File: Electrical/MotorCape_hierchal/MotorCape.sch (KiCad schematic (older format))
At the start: 9 parts, among them J11 flag_wheel servo, J7 i2c bus connector, P13 battery_connector, P14 Pi_Connector, U1 IMU

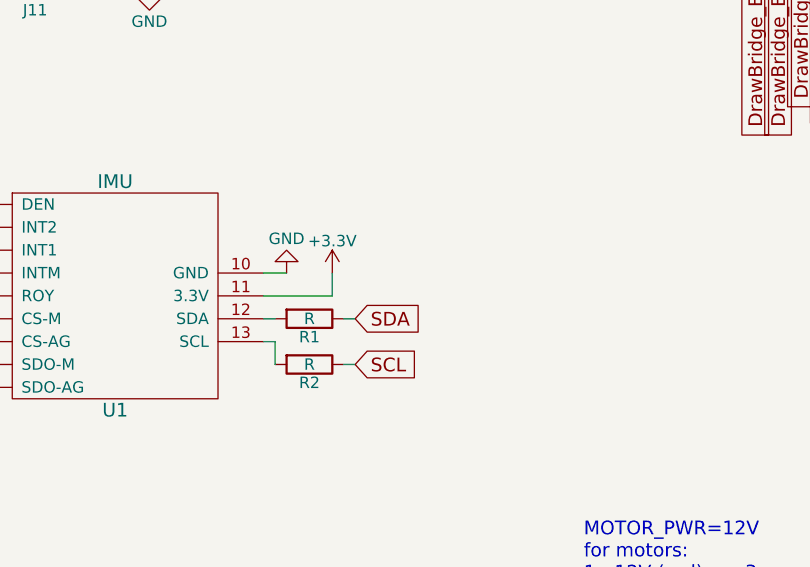
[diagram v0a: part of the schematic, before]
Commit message: trying to lay-out things. lots of via's, this could be a bit messy
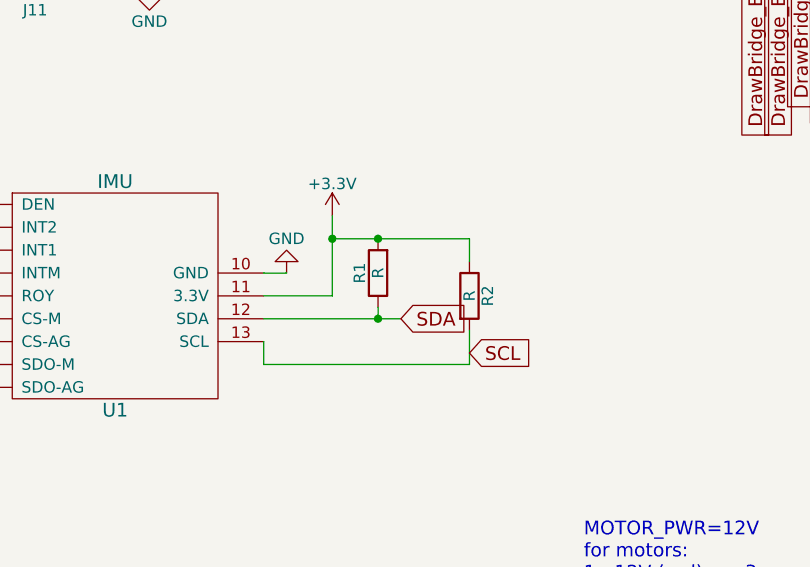
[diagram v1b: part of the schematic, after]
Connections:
- net +3V3: now also R1.2, R2.1
- net SCL: now also R2.2, U1.13 (SCL); no longer R2.1
- net SDA: now also U1.12 (SDA)
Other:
- moved on the sheet: R1, R2
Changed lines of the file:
@@
 NoConn ~ 4300 5900
 NoConn ~ 4300 6000
-Text GLabel 6000 5700 2    60   Input ~ 0
+Text GLabel 6200 5700 2    60   Input ~ 0
 SDA
-Text GLabel 6000 5900 2    60   Input ~ 0
+Text GLabel 6500 5850 2    60   Input ~ 0
 SCL
 $Comp
@@
 L R R2
 U 1 1 5ACFD3ED
-P 5800 5900
-F 0 "R2" V 5880 5900 50  0000 C CNN
-F 1 "R" V 5800 5900 50  0000 C CNN
-F 2 "Resistors_THT:R_Axial_DIN0204_L3.6mm_D1.6mm_P5.08mm_Horizontal" V 5730 5900 50  0001 C CNN
-F 3 "" H 5800 5900 50  0001 C CNN
-	1    5800 5900
-	0    1    1    0
-$EndComp
-$Comp
-L R R1
-U 1 1 5ACFD510
-P 5800 5700
-F 0 "R1" V 5880 5700 50  0000 C CNN
-F 1 "R" V 5800 5700 50  0000 C CNN
-F 2 "Resistors_THT:R_Axial_DIN0204_L3.6mm_D1.6mm_P5.08mm_Horizontal" V 5730 5700 50  0001 C CNN
-F 3 "" H 5800 5700 50  0001 C CNN
-	1    5800 5700
-	0    1    1    0
+P 6500 5600
+F 0 "R2" V 6580 5600 50  0000 C CNN
+F 1 "R" V 6500 5600 50  0000 C CNN
+F 2 "Resistors_THT:R_Axial_DIN0204_L3.6mm_D1.6mm_P5.08mm_Horizontal" V 6430 5600 50  0001 C CNN
+F 3 "" H 6500 5600 50  0001 C CNN
+	1    6500 5600
+	1    0    0    -1
 $EndComp
 Text GLabel 10550 1400 1    60   Input ~ 0
@@
 L +3.3V #PWR011
 U 1 1 5ACCD4EB
-P 5900 5500
-F 0 "#PWR011" H 5900 5350 50  0001 C CNN
-F 1 "+3.3V" H 5900 5640 50  0000 C CNN
-F 2 "" H 5900 5500 50  0001 C CNN
-F 3 "" H 5900 5500 50  0001 C CNN
-	1    5900 5500
+P 5900 5250
+F 0 "#PWR011" H 5900 5100 50  0001 C CNN
+F 1 "+3.3V" H 5900 5390 50  0000 C CNN
+F 2 "" H 5900 5250 50  0001 C CNN
+F 3 "" H 5900 5250 50  0001 C CNN
+	1    5900 5250
 	1    0    0    -1
 $EndComp
@@
 	5700 5500 5600 5500
 Wire Wire Line
-	5900 5500 5900 5600
+	5900 5250 5900 5600
 Wire Wire Line
 	5900 5600 5600 5600
 Wire Wire Line
-	5650 5700 5600 5700
-Wire Wire Line
-	5600 5800 5650 5800
-Wire Wire Line
-	5650 5800 5650 5900
-Wire Wire Line
-	6000 5700 5950 5700
-Wire Wire Line
-	6000 5900 5950 5900
+	5600 5700 6200 5700
 Wire Wire Line
 	5050 3900 5000 3900
@@
 	0    1    1    0
 $EndComp
+$Comp
+L R R1
+U 1 1 5ACFD510
+P 6100 5500
+F 0 "R1" V 6180 5500 50  0000 C CNN
+F 1 "R" V 6100 5500 50  0000 C CNN
+F 2 "Resistors_THT:R_Axial_DIN0204_L3.6mm_D1.6mm_P5.08mm_Horizontal" V 6030 5500 50  0001 C CNN
+F 3 "" H 6100 5500 50  0001 C CNN
+	1    6100 5500
+	-1   0    0    1
+$EndComp
+Wire Wire Line
+	5900 5350 6500 5350
+Connection ~ 5900 5350
+Wire Wire Line
+	6100 5650 6100 5700
+Connection ~ 6100 5700
+Wire Wire Line
+	6500 5900 6500 5750
+Wire Wire Line
+	6500 5350 6500 5450
+Connection ~ 6100 5350
+Wire Wire Line
+	5600 5900 6500 5900
+Wire Wire Line
+	5600 5800 5600 5900
 $EndSCHEMATC

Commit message: pushing changes while routing. still not done yet
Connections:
- net BackLeft_DIR: now also ARD1.59 (D28); no longer ARD1.56 (D25)
- net BackLeft_ENC_A: now also ARD1.61 (D30); no longer ARD1.57 (D26)
- net BackLeft_ENC_B: now also ARD1.63 (D32); no longer ARD1.58 (D27)
- net BackRight_DIR: now also ARD1.71 (D40); no longer ARD1.62 (D31)
- net BackRight_ENC_A: now also ARD1.73 (D42); no longer ARD1.63 (D32)
- net BackRight_ENC_B: now also ARD1.75 (D44); no longer ARD1.64 (D33)
- net DrawBridge_DIR: now also ARD1.82 (D51); no longer ARD1.68 (D37)
- net DrawBridge_ENC_A: now also ARD1.83 (D52_CS2); no longer ARD1.69 (D38)
- net DrawBridge_ENC_B: now also ARD1.84 (D53); no longer ARD1.70 (D39)
- net FlagWheel_DIR: now also ARD1.77 (D46); no longer ARD1.65 (D34)
- net FlagWheel_ENC_A: now also ARD1.79 (D48); no longer ARD1.66 (D35)
- net FlagWheel_ENC_B: now also ARD1.81 (D50); no longer ARD1.67 (D36)
- net FrontLeft_ENC_A: now also ARD1.55 (D24); no longer ARD1.54 (D23)
- net FrontLeft_ENC_B: now also ARD1.57 (D26); no longer ARD1.55 (D24)
- net FrontRight_DIR: now also ARD1.65 (D34); no longer ARD1.59 (D28)
- net FrontRight_ENC_A: now also ARD1.67 (D36); no longer ARD1.60 (D29)
- net FrontRight_ENC_B: now also ARD1.69 (D38); no longer ARD1.61 (D30)
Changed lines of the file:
@@
 	-1   0    0    -1
 $EndComp
-NoConn ~ 6350 4000
-NoConn ~ 6450 4000
-NoConn ~ 6550 4000
-NoConn ~ 6650 4000
 NoConn ~ 6750 4000
-NoConn ~ 6850 4000
 NoConn ~ 6950 4000
-NoConn ~ 7050 4000
 NoConn ~ 7150 4000
-NoConn ~ 7250 4000
 NoConn ~ 7350 4000
-NoConn ~ 7450 4000
 NoConn ~ 7550 4000
-NoConn ~ 7650 4000
 NoConn ~ 9550 4000
 NoConn ~ 9650 4000
-NoConn ~ 9750 4000
-NoConn ~ 9850 4000
-NoConn ~ 9950 4000
 NoConn ~ 6350 1400
 NoConn ~ 6450 1400
@@
 Text GLabel 10650 4000 3    60   Input ~ 0
 FrontLeft_SPD
-Text GLabel 9150 4000 3    60   Input ~ 0
+Text GLabel 8850 4000 3    60   Input ~ 0
 BackLeft_DIR
 Text GLabel 10550 4000 3    60   Input ~ 0
 BackLeft_SPD
-Text GLabel 9350 4000 3    60   Input ~ 0
+Text GLabel 9250 4000 3    60   Input ~ 0
 FrontLeft_ENC_A
-Text GLabel 9250 4000 3    60   Input ~ 0
+Text GLabel 9050 4000 3    60   Input ~ 0
 FrontLeft_ENC_B
-Text GLabel 9050 4000 3    60   Input ~ 0
+Text GLabel 8650 4000 3    60   Input ~ 0
 BackLeft_ENC_A
-Text GLabel 8950 4000 3    60   Input ~ 0
+Text GLabel 8450 4000 3    60   Input ~ 0
 BackLeft_ENC_B
 Text GLabel 10450 4000 3    60   Input ~ 0
@@
 Text GLabel 10350 4000 3    60   Input ~ 0
 BackRight_SPD
-Text GLabel 8250 4000 3    60   Input ~ 0
+Text GLabel 7050 4000 3    60   Input ~ 0
 FlagWheel_DIR
 Text GLabel 10250 4000 3    60   Input ~ 0
 FlagWheel_SPD
-Text GLabel 7950 4000 3    60   Input ~ 0
+Text GLabel 6550 4000 3    60   Input ~ 0
 DrawBridge_DIR
 Text GLabel 10150 4000 3    60   Input ~ 0
 DrawBridge_SPD
-Text GLabel 8150 4000 3    60   Input ~ 0
+Text GLabel 6850 4000 3    60   Input ~ 0
 FlagWheel_ENC_A
+Text GLabel 6650 4000 3    60   Input ~ 0
+FlagWheel_ENC_B
+Text GLabel 6450 4000 3    60   Input ~ 0
+DrawBridge_ENC_A
+Text GLabel 6350 4000 3    60   Input ~ 0
+DrawBridge_ENC_B
+Text GLabel 8250 4000 3    60   Input ~ 0
+FrontRight_DIR
 Text GLabel 8050 4000 3    60   Input ~ 0
-FlagWheel_ENC_B
+FrontRight_ENC_A
 Text GLabel 7850 4000 3    60   Input ~ 0
-DrawBridge_ENC_A
-Text GLabel 7750 4000 3    60   Input ~ 0
-DrawBridge_ENC_B
-Text GLabel 8850 4000 3    60   Input ~ 0
-FrontRight_DIR
-Text GLabel 8750 4000 3    60   Input ~ 0
-FrontRight_ENC_A
-Text GLabel 8650 4000 3    60   Input ~ 0
 FrontRight_ENC_B
-Text GLabel 8550 4000 3    60   Input ~ 0
+Text GLabel 7650 4000 3    60   Input ~ 0
 BackRight_DIR
-Text GLabel 8450 4000 3    60   Input ~ 0
+Text GLabel 7450 4000 3    60   Input ~ 0
 BackRight_ENC_A
-Text GLabel 8350 4000 3    60   Input ~ 0
+Text GLabel 7250 4000 3    60   Input ~ 0
 BackRight_ENC_B
 Text GLabel 10050 4000 3    60   Input ~ 0
@@
 	7250 1150 7250 1400
 $Comp
+L R R1
+U 1 1 5ACFD510
+P 6100 5500
+F 0 "R1" V 6180 5500 50  0000 C CNN
+F 1 "R" V 6100 5500 50  0000 C CNN
+F 2 "Resistors_THT:R_Axial_DIN0204_L3.6mm_D1.6mm_P5.08mm_Horizontal" V 6030 5500 50  0001 C CNN
+F 3 "" H 6100 5500 50  0001 C CNN
+	1    6100 5500
+	-1   0    0    1
+$EndComp
+Wire Wire Line
+	5900 5350 6500 5350
+Connection ~ 5900 5350
+Wire Wire Line
+	6100 5650 6100 5700
+Connection ~ 6100 5700
+Wire Wire Line
+	6500 5900 6500 5750
+Wire Wire Line
+	6500 5350 6500 5450
+Connection ~ 6100 5350
+Wire Wire Line
+	5600 5900 6500 5900
+Wire Wire Line
+	5600 5800 5600 5900
+NoConn ~ 7750 4000
+NoConn ~ 7950 4000
+NoConn ~ 8150 4000
+NoConn ~ 8350 4000
+NoConn ~ 8550 4000
+NoConn ~ 8750 4000
+NoConn ~ 8950 4000
+NoConn ~ 9150 4000
+NoConn ~ 9350 4000
+NoConn ~ 9750 4000
+$Comp
 L Arduino_Due_Shield ARD1
 U 1 1 5AC90C45
@@
 	0    1    1    0
 $EndComp
-$Comp
-L R R1
-U 1 1 5ACFD510
-P 6100 5500
-F 0 "R1" V 6180 5500 50  0000 C CNN
-F 1 "R" V 6100 5500 50  0000 C CNN
-F 2 "Resistors_THT:R_Axial_DIN0204_L3.6mm_D1.6mm_P5.08mm_Horizontal" V 6030 5500 50  0001 C CNN
-F 3 "" H 6100 5500 50  0001 C CNN
-	1    6100 5500
-	-1   0    0    1
-$EndComp
-Wire Wire Line
-	5900 5350 6500 5350
-Connection ~ 5900 5350
-Wire Wire Line
-	6100 5650 6100 5700
-Connection ~ 6100 5700
-Wire Wire Line
-	6500 5900 6500 5750
-Wire Wire Line
-	6500 5350 6500 5450
-Connection ~ 6100 5350
-Wire Wire Line
-	5600 5900 6500 5900
-Wire Wire Line
-	5600 5800 5600 5900
+NoConn ~ 9850 4000
+NoConn ~ 9950 4000
 $EndSCHEMATC

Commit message: pushing latest motor controller layout changes
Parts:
- removed J7: i2c bus connector, MotorCapeComponents:Pin_Header_Latched_1x02, symbol Conn_01x02
- renumbered P14 to Pi_Bus1, J11 to servo1
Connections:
- net BackRight_DIR: now also ARD1.82 (D51); no longer ARD1.71 (D40)
- net BackRight_ENC_A: now also ARD1.83 (D52_CS2); no longer ARD1.73 (D42)
- net BackRight_ENC_B: now also ARD1.84 (D53); no longer ARD1.75 (D44)
- net DrawBridge_DIR: now also ARD1.73 (D42); no longer ARD1.82 (D51)
- net DrawBridge_ENC_A: now also ARD1.75 (D44); no longer ARD1.83 (D52_CS2)
- net DrawBridge_ENC_B: now also ARD1.77 (D46); no longer ARD1.84 (D53)
- net FlagWheel_DIR: now also ARD1.67 (D36); no longer ARD1.77 (D46)
- net FlagWheel_ENC_A: now also ARD1.69 (D38); no longer ARD1.79 (D48)
- net FlagWheel_ENC_B: now also ARD1.71 (D40); no longer ARD1.81 (D50)
- net FrontRight_ENC_A: now also ARD1.79 (D48); no longer ARD1.67 (D36)
- net FrontRight_ENC_B: now also ARD1.81 (D50); no longer ARD1.69 (D38)
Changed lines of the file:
@@
 MOTOR_PWR=12V\nfor motors:\n1 - 12V (red)       3 - encoder gnd(green)       5 - encoder A (yellow)\n2 - Gnd (black)     4 - encoder Vcc(5V)(blue)    6 - encoder B (white)\n
 $Comp
-L Conn_01x02 J7
-U 1 1 59FC44BE
-P 4550 2450
-F 0 "J7" H 4550 2250 50  0000 C CNN
-F 1 "i2c bus connector" H 4600 2600 50  0000 C CNN
-F 2 "MotorCapeComponents:Pin_Header_Latched_1x02" H 4550 2450 50  0001 C CNN
-F 3 "" H 4550 2450 50  0001 C CNN
-	1    4550 2450
-	-1   0    0    -1
-$EndComp
-$Comp
-L Conn_01x03 J11
+L Conn_01x03 servo1
 U 1 1 5A0ED002
 P 4600 4150
-F 0 "J11" H 4600 3950 50  0000 C CNN
+F 0 "servo1" H 4600 3950 50  0000 C CNN
 F 1 "flag_wheel servo" H 4550 4350 50  0000 C CNN
 F 2 "MotorCapeComponents:Pin_Header_Latched_1x03" H 4600 4150 50  0001 C CNN
@@
 NoConn ~ 10050 1400
 NoConn ~ 9950 1400
-Text GLabel 4800 2450 2    60   Input ~ 0
-SCL
-Text GLabel 4800 2550 2    60   Input ~ 0
-SDA
 Text GLabel 9550 1400 1    60   Input ~ 0
 SCL
@@
 NoConn ~ 7650 1500
 $Comp
-L CONN_01X04 P14
+L CONN_01X04 Pi_Bus1
 U 1 1 5AA1DD33
 P 4550 3150
-F 0 "P14" H 4550 2900 50  0000 C CNN
+F 0 "Pi_Bus1" H 4550 2900 50  0000 C CNN
 F 1 "Pi_Connector" H 4550 3400 50  0000 C CNN
 F 2 "MotorCapeComponents:Pin_Header_Latched_1x04" H 4550 3150 50  0001 C CNN
@@
 Text GLabel 10350 4000 3    60   Input ~ 0
 BackRight_SPD
-Text GLabel 7050 4000 3    60   Input ~ 0
+Text GLabel 8050 4000 3    60   Input ~ 0
 FlagWheel_DIR
 Text GLabel 10250 4000 3    60   Input ~ 0
 FlagWheel_SPD
-Text GLabel 6550 4000 3    60   Input ~ 0
+Text GLabel 7450 4000 3    60   Input ~ 0
 DrawBridge_DIR
 Text GLabel 10150 4000 3    60   Input ~ 0
 DrawBridge_SPD
-Text GLabel 6850 4000 3    60   Input ~ 0
+Text GLabel 7850 4000 3    60   Input ~ 0
 FlagWheel_ENC_A
-Text GLabel 6650 4000 3    60   Input ~ 0
+Text GLabel 7650 4000 3    60   Input ~ 0
 FlagWheel_ENC_B
-Text GLabel 6450 4000 3    60   Input ~ 0
+Text GLabel 7250 4000 3    60   Input ~ 0
 DrawBridge_ENC_A
-Text GLabel 6350 4000 3    60   Input ~ 0
+Text GLabel 7050 4000 3    60   Input ~ 0
 DrawBridge_ENC_B
 Text GLabel 8250 4000 3    60   Input ~ 0
 FrontRight_DIR
-Text GLabel 8050 4000 3    60   Input ~ 0
+Text GLabel 6850 4000 3    60   Input ~ 0
 FrontRight_ENC_A
-Text GLabel 7850 4000 3    60   Input ~ 0
+Text GLabel 6650 4000 3    60   Input ~ 0
 FrontRight_ENC_B
-Text GLabel 7650 4000 3    60   Input ~ 0
+Text GLabel 6550 4000 3    60   Input ~ 0
 BackRight_DIR
-Text GLabel 7450 4000 3    60   Input ~ 0
+Text GLabel 6450 4000 3    60   Input ~ 0
 BackRight_ENC_A
-Text GLabel 7250 4000 3    60   Input ~ 0
+Text GLabel 6350 4000 3    60   Input ~ 0
 BackRight_ENC_B
 Text GLabel 10050 4000 3    60   Input ~ 0
@@
 	4800 3300 4750 3300
 Wire Wire Line
-	4800 2450 4750 2450
-Wire Wire Line
-	4750 2550 4800 2550
-Wire Wire Line
 	5700 5500 5600 5500
